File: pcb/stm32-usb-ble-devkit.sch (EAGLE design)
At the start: 98 parts, among them CN1 USB-MICROB-2TABS, CN2 USB-C-2.0-FEMALE, CN3 USB-C-2.0-FEMALE, Q2 AO3402, Q4 AO3401, Q6 AO3401, Q8 AO3401, U1 STM32F103-48LQFP, U2 STM32F205-64, U3 TUSB320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

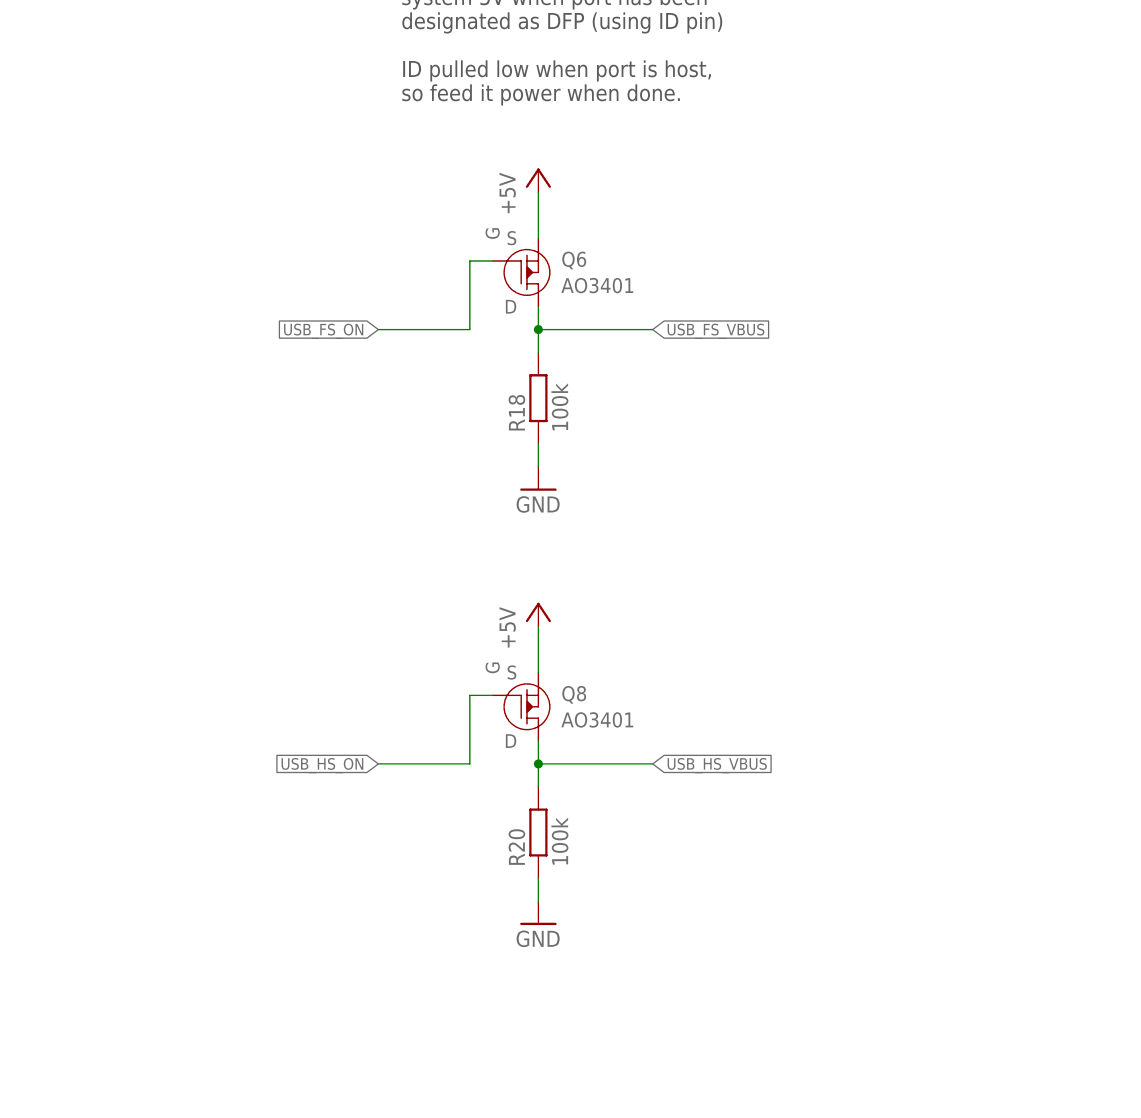
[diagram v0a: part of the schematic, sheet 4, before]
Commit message: pcb: Switch OTG PSU MOSFET to dedicated IC
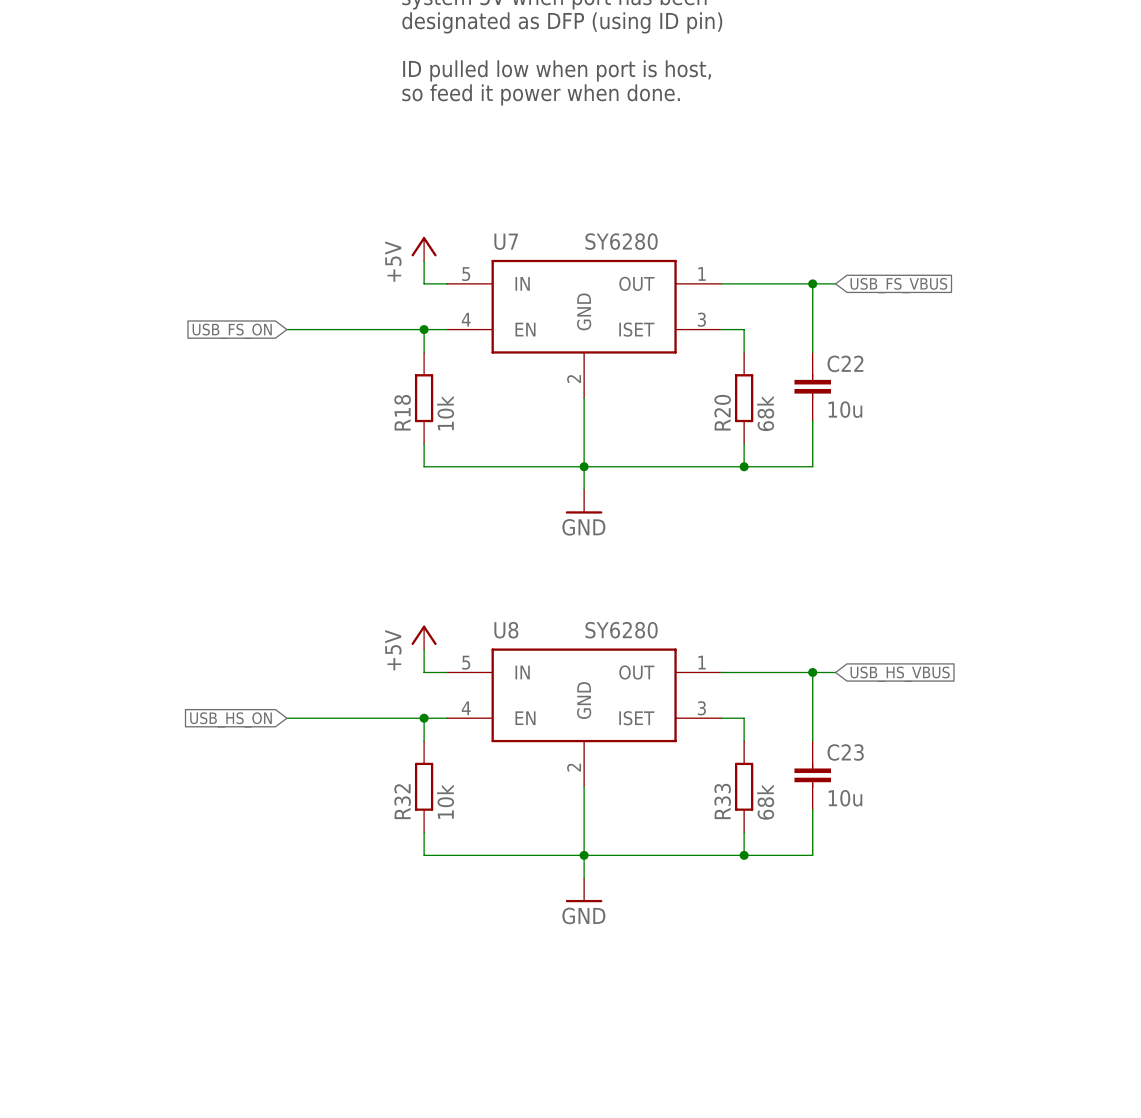
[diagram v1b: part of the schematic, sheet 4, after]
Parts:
- removed Q6, Q8: AO3401, tuetuopay:AO3401
- added C22, C23: 10u, tuetuopay:C0603
- added R32: 10k, tuetuopay:RR0603
- added R33: 68k, tuetuopay:RR0603
- added U7, U8: SY6280, tuetuopay:SY6280
- R18: value 100k -> 10k
- R20: value 100k -> 68k
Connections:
- new net USB_FS_ISET: R20.2, U7.ISET
- new net USB_HS_ISET: R33.2, U8.ISET
- net +5V: now also U7.IN, U8.IN; no longer Q6.S, Q8.S
- net GND: now also C22.2, C23.2, R32.1, R33.1, U7.GND, U8.GND
- net USB_FS_ON: now also R18.2, U7.EN; no longer Q6.G
- net USB_FS_VBUS: now also C22.1, U7.OUT; no longer Q6.D, R18.2
- net USB_HS_ON: now also R32.2, U8.EN; no longer Q8.G
- net USB_HS_VBUS: now also C23.1, U8.OUT; no longer Q8.D, R20.2
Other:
- moved on the sheet: R18, R20
